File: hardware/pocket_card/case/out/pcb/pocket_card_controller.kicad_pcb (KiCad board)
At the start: 2 copper layers, 80.5 x 37 mm, 19 parts, among them U1 SOIC-28W_7.5x17.9mm_P1.27mm

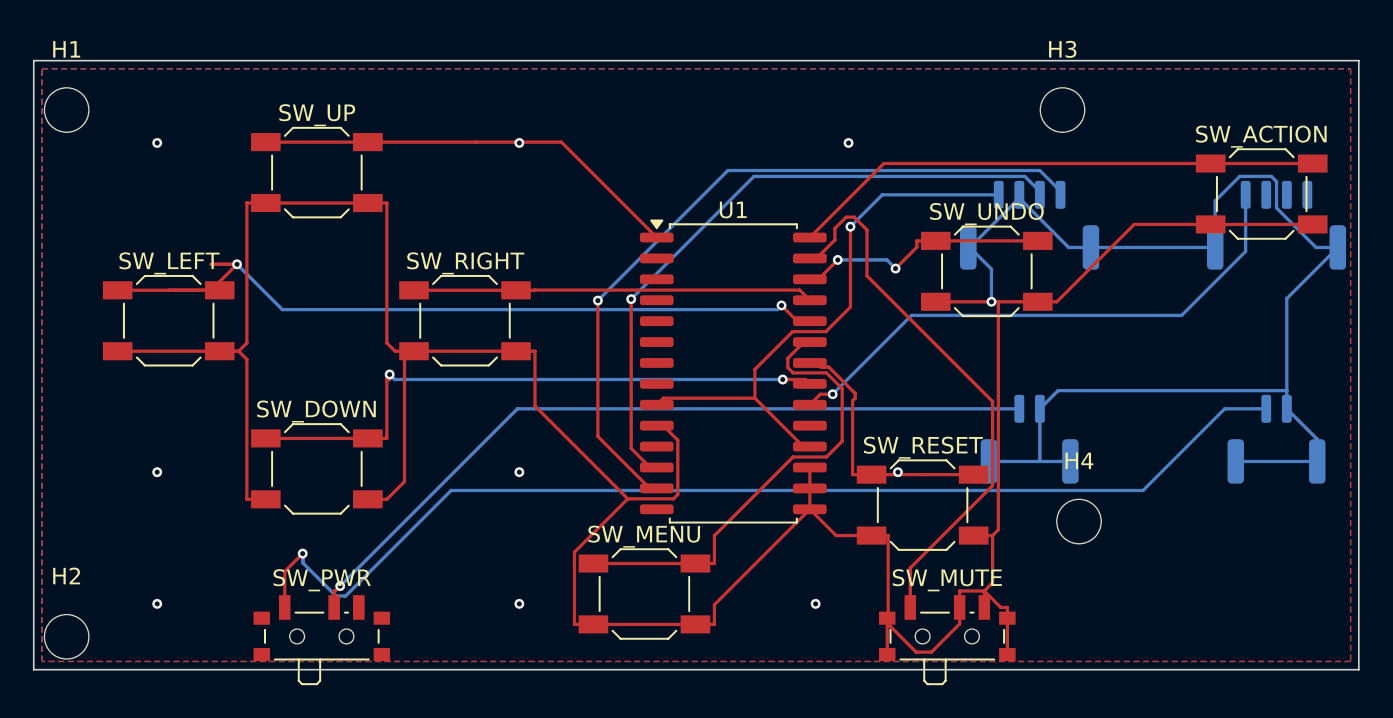
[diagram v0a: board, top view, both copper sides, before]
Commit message: Add PuzzlePocket decorative silkscreen to the controller PCB.
Rasterized brick/rules/logo/label artwork (HTML paint order, in-place back
glyph flip) so knockouts stay aligned and IO labels stay on the JST pads.

Co-authored-by: Cursor <cursoragent@cursor.com>
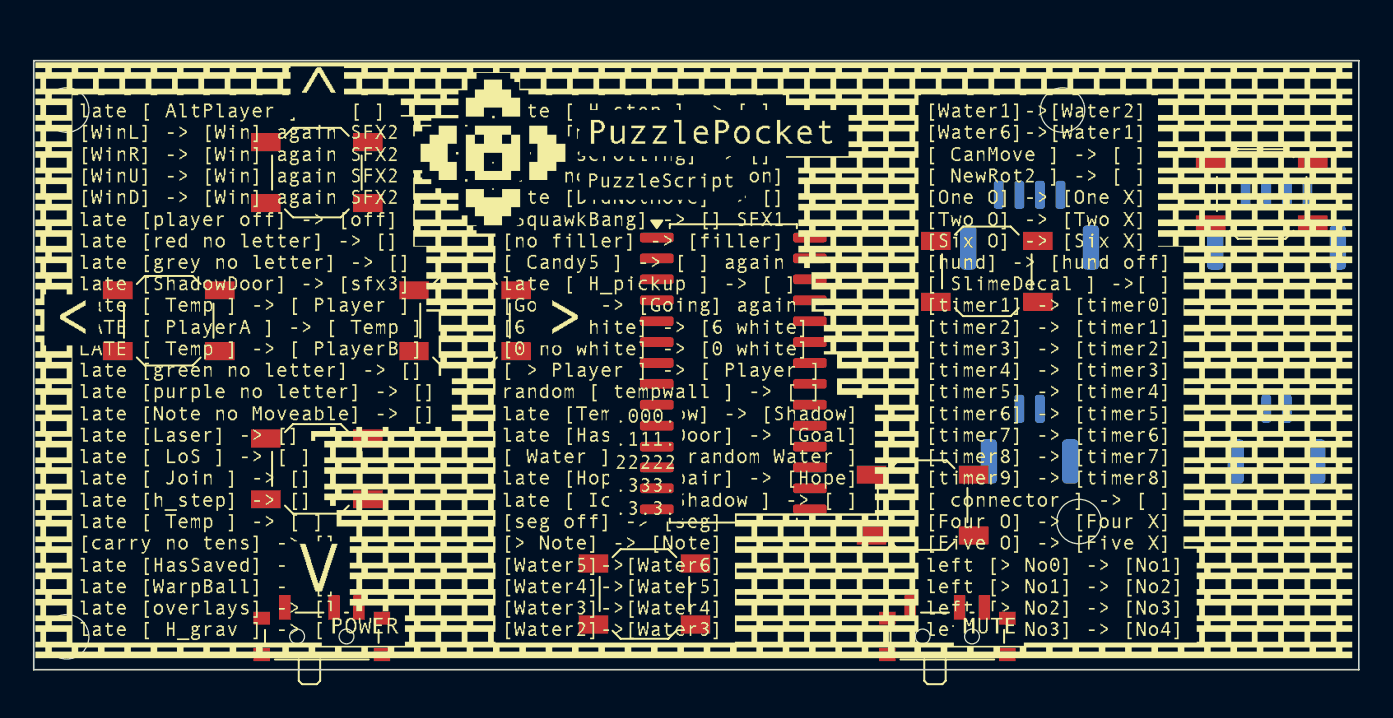
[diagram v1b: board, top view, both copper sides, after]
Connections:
- J_BAT_IN pad 1: BAT_P -> (no net)
- J_BAT_IN pad 2: GND -> (no net)
- J_BAT_IN pad MP: GND -> (no net)
- J_BAT_OUT pad 1: BAT_SW -> (no net)
- J_BAT_OUT pad 2: GND -> (no net)
- J_BAT_OUT pad MP: GND -> (no net)
- J_EXP pad 1: INT -> (no net)
- J_EXP pad MP: GND -> (no net)
- J_I2C pad 1: +3V3 -> (no net)
- J_I2C pad 2: GND -> (no net)
- J_I2C pad 3: SCL -> (no net)
- J_I2C pad 4: SDA -> (no net)
- J_I2C pad MP: GND -> (no net)
- SW_ACTION pad 1: SIG_ACTION -> (no net)
- SW_ACTION pad 2: GND -> (no net)
- SW_DOWN pad 1: SIG_DOWN -> (no net)
- SW_DOWN pad 2: GND -> (no net)
- SW_LEFT pad 1: SIG_LEFT -> (no net)
- SW_LEFT pad 2: GND -> (no net)
- SW_MENU pad 1: SIG_MENU -> (no net)
- SW_MENU pad 2: GND -> (no net)
- SW_MUTE pad : GND -> (no net)
- SW_MUTE pad 1: SIG_MUTE -> (no net)
- SW_MUTE pad 2: GND -> (no net)
- SW_MUTE pad 3: GND -> (no net)
- SW_PWR pad 1: BAT_SW -> (no net)
- SW_PWR pad 2: BAT_P -> (no net)
- SW_RESET pad 1: SIG_RESET -> (no net)
- SW_RESET pad 2: GND -> (no net)
- SW_RIGHT pad 1: SIG_RIGHT -> (no net)
- SW_RIGHT pad 2: GND -> (no net)
- SW_UNDO pad 1: SIG_UNDO -> (no net)
- SW_UNDO pad 2: GND -> (no net)
- SW_UP pad 1: SIG_UP -> (no net)
- SW_UP pad 2: GND -> (no net)
- U1 pad 1: SIG_UP -> (no net)
- U1 pad 10: GND -> (no net)
- U1 pad 12: SCL -> (no net)
- U1 pad 13: SDA -> (no net)
- U1 pad 15: GND -> (no net)
- U1 pad 16: GND -> (no net)
- U1 pad 17: GND -> (no net)
- U1 pad 18: +3V3 -> (no net)
- U1 pad 20: INT -> (no net)
- U1 pad 21: SIG_DOWN -> (no net)
- U1 pad 22: SIG_RESET -> (no net)
- U1 pad 23: SIG_MENU -> (no net)
- U1 pad 24: SIG_LEFT -> (no net)
- U1 pad 25: SIG_RIGHT -> (no net)
- U1 pad 26: SIG_UNDO -> (no net)
- U1 pad 27: SIG_MUTE -> (no net)
- U1 pad 28: SIG_ACTION -> (no net)
- U1 pad 9: +3V3 -> (no net)
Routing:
- net GND: track 263.2 -> 0.00 mm, vias 8 -> 0
- net BAT_SW: track 69.5 -> 0.00 mm, vias 1 -> 0
- net SIG_LEFT: track 50.9 -> 0.00 mm, vias 2 -> 0
- net BAT_P: track 47.2 -> 0.00 mm, vias 1 -> 0
- net SDA: track 45.3 -> 0.00 mm, vias 1 -> 0
- net SCL: track 39.6 -> 0.00 mm, vias 1 -> 0
- net SIG_DOWN: track 37.7 -> 0.00 mm, vias 2 -> 0
- net +3V3: track 34.5 -> 0.00 mm, vias 1 -> 0
- net INT: track 33.8 -> 0.00 mm, vias 1 -> 0
- net SIG_MUTE: track 33.4 -> 0.00 mm
- net SIG_ACTION: track 32.4 -> 0.00 mm
- net SIG_MENU: track 28.5 -> 0.00 mm
- net SIG_UP: track 26.2 -> 0.00 mm, vias 1 -> 0
- net SIG_RIGHT: track 24.3 -> 0.00 mm
- net SIG_RESET: track 16.1 -> 0.00 mm, vias 1 -> 0
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- removed copper zone on B.Cu, net GND
- removed copper zone on F.Cu, net GND
